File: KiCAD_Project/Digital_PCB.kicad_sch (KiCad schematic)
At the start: 40 parts, among them J1 NP_Conn_01x02_Relief, J10 1-0001156, J2 Board to Board, J3 1-0001156, J4 1-0001205, J5 NP_Conn_01x04, J6 NP_Conn_01x02_Relief, J7 NP_Conn_01x04, U1 1-0000207, Y1 1-0000721

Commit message: Schematic ERC Issue Cleanup
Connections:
- no-connect marks 12 -> 13
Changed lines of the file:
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@@
 	)
 	(no_connect
+		(at 119.38 91.44)
+	)
+	(no_connect
 		(at 152.4 119.38)
 	)
@@
 			"AAAAAAAAAAAAAAAAAAAAAAAAAAAAAAAAAAAAAAAAAAAAAAAAAAAAAAAAAAAAAAAAAAAAAAAAAAAA"
 			"AAAAAAAAAAAAAAAAAAAAAAAAAAAAAAAAAAAAAAAAAAAAAAAAAAAAAAAAAAAAAAAAAAAAAAAAAAAA"
+			"AAAAAAAAAAAAAAAAAAAAAAAAAAAAAAAAAAAAAAAAAAAAAAAAAAAAAAAAAAAAAAAAAAAAAAAAAAAA"
+			"AAAAAAAAAAAAAAAAAAAAAAAAAAAAAAAAAAAAAAAAAAAAAAAAAAAAAAAAAAAAAAAAAAAAAAAAAAAA"
+			"AAAAAAAAAAAAAAAAAAAAAAAAAAAAAAAAAAAAAAAAAAAAAAAAAAAAAAAAAAAAAAAAAAAAAAAAAAAA"
+			"AAAAAAAAAAAAAAAAAAAAAAAAAAAAAAAAAAAAAAAAAAAAAAAAAAAAAAAAAAAAAAAAAAAAAAAAAAAA"
+			"AAAAAAAAAAAAAAAAAAAAAAAAAAAAAAAAAAAAAAAAAAAAAAAAAAAAAAAAAAAAAAAAAAAAAAAAAAAA"
+			"AAAAAAAAAAAAAAAAAAAAAAAAAAAAAAAAAAAAAAAAAAAAAAAAAAAAAAAAAAAAAAAAAAAAAAAAAAAA"
+			"AAAAAAAAAAAAAAAAAAAAAAAAAAAAAAAAAAAAAAAAAAAAAAAAAAAAAAAAAAAAAAAAAAAAAAAAAAAA"
+			"AAAAAAAAAAAAAAAAAAAAAAAAAAAAAAAAAAAAAAAAAAAAAAAAAAAAAAAAAAAAAAAAAAAAAAAAAAAA"
+			"AAAAAAAAAAAAAAAAAAAAAAAAAAAAAAAAAAAAAAAAAAAAAAAAAAAAAAAAAAAAAAAAAAAAAAAAAAAA"
+			"AAAAAAAAAAAAAAAAAAAAAAAAAAAAAAAAAAAAAAAAAAAAAAAAAAAAAAAAAAAAAAAAAAAAAAAAAAAA"
+			"AAAAAAAAAAAAAAAAAAAAAAAAAAAAAAAAAAAAAAAAAAAAAAAAAAAAAAAAAAAAAAAAAAAAAAAAAAAA"
+			"AAAAAAAAAAAAAAAAAAAAAAAAAAAAAAAAAAAAAAAAAAAAAAAAAAAAAAAAAAAAAAAAAAAAAAAAAAAA"
+			"AAAAAAAAAAAAAAAAAAAAAAAAAAAAAAAAAAAAAAAAAAAAAAAAAAAAAAAAAAAAAAAAAAAAAAAAAAAA"
+			"AAAAAAAAAAAAAAAAAAAAAAAAAAAAAAAAAAAAAAAAAAAAAAAAAAAAAAAAAAAAAAAAAAAAAAAAAAAA"
+			"AAAAAAAAAAAAAAAAAAAAAAAAAAAAAAAAAAAAAAAAAAAAAAAAAAAAAAAAAAAAAAAAAAAAAAAAAAAA"
+			"AAAAAAAAAAAAAAAAAAAAAAAAAAAAAAAAAAAAAAAAAAAAAAAAAAAAAAAAAAAAAAAAAAAAAAAAAAAA"
+			"AAAAAAAAAAAAAAAAAAAAAAAAAAAAAAAAAAAAAAAAAAAAAAAAAAAAAAAAAAAAAAAAAAAAAAAAAAAA"
+			"AAAAAAAAAAAAAAAAAAAAAAAAAAAAAAAAAAAAAAAAAAAAAAAAAAAAAAAAAAAAAAAAAAAAAAAAAAAA"
 			"AAAAAAAAAA=="
 		)
@@
 	(symbol
 		(lib_id "power:PWR_FLAG")
-		(at -22.86 194.31 0)
+		(at 5.08 19.05 0)
 		(unit 1)
 		(exclude_from_sim no)
@@
 		(fields_autoplaced yes)
 		(property "Reference" "#FLG04"
-			(at -22.86 192.405 0)
+			(at 5.08 17.145 0)
 			(effects
 				(font
@@
 		)
 		(property "Value" "PWR_FLAG"
-			(at -22.86 189.23 0)
+			(at 5.08 13.97 0)
 			(effects
 				(font
@@
 		)
 		(property "Footprint" ""
-			(at -22.86 194.31 0)
+			(at 5.08 19.05 0)
 			(effects
 				(font
@@
 		)
 		(property "Datasheet" "~"
-			(at -22.86 194.31 0)
+			(at 5.08 19.05 0)
 			(effects
 				(font
@@
 		)
 		(property "Description" "Special symbol for telling ERC where power comes from"
-			(at -22.86 194.31 0)
+			(at 5.08 19.05 0)
 			(effects
 				(font
@@
 	(symbol
 		(lib_id "power:GND")
-		(at -22.86 194.31 0)
+		(at 5.08 19.05 0)
 		(unit 1)
 		(exclude_from_sim no)
@@
 		(dnp no)
 		(property "Reference" "#PWR052"
-			(at -22.86 200.66 0)
+			(at 5.08 25.4 0)
 			(effects
 				(font
@@
 		)
 		(property "Value" "GND"
-			(at -22.733 198.7042 0)
+			(at 5.207 23.4442 0)
 			(effects
 				(font
@@
 		)
 		(property "Footprint" ""
-			(at -22.86 194.31 0)
+			(at 5.08 19.05 0)
 			(effects
 				(font
@@
 		)
 		(property "Datasheet" ""
-			(at -22.86 194.31 0)
+			(at 5.08 19.05 0)
 			(effects
 				(font
@@
 		)
 		(property "Description" "Power symbol creates a global label with name \"GND\" , ground"
-			(at -22.86 194.31 0)
+			(at 5.08 19.05 0)
 			(effects
 				(font

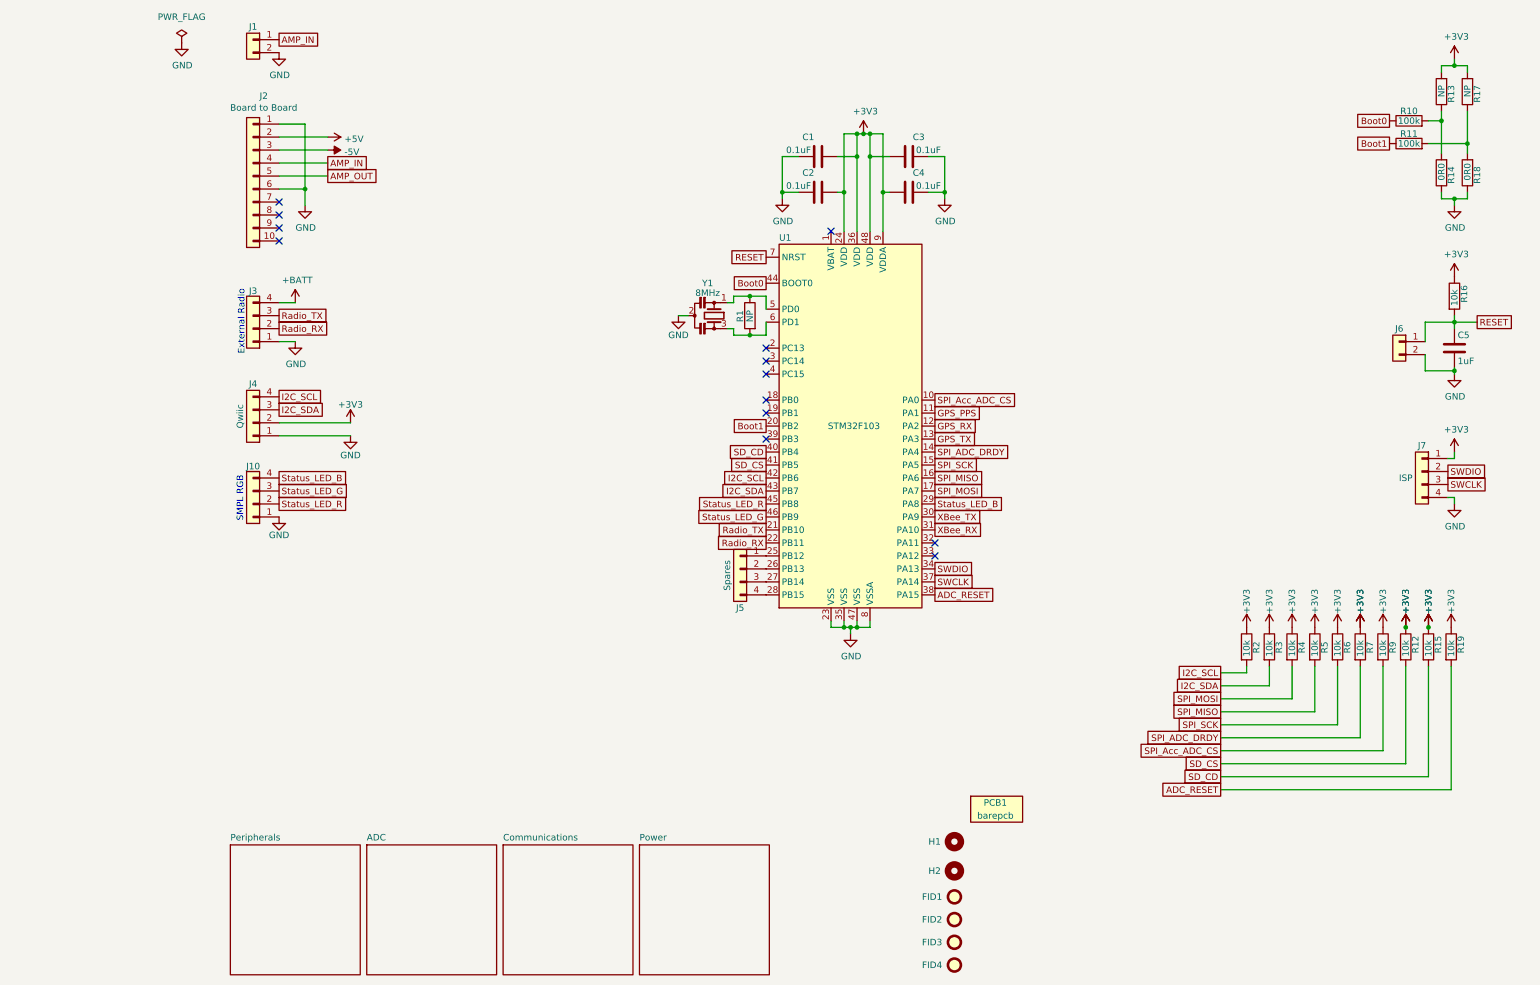
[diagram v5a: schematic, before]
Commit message: Revised Layout for Rev2.0 Changes
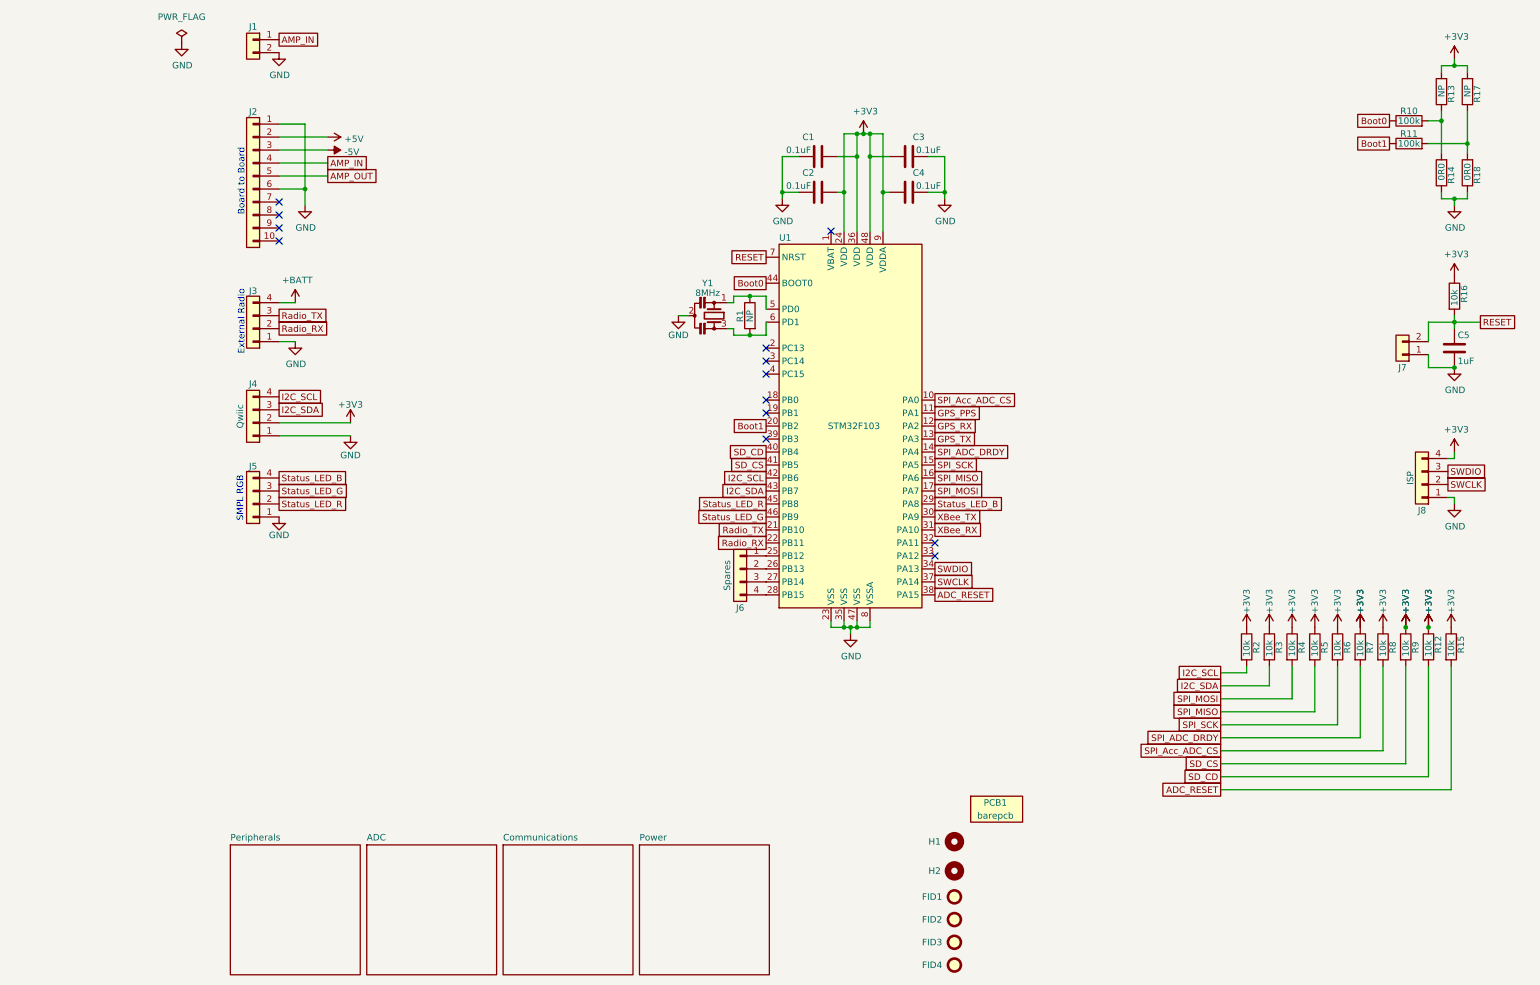
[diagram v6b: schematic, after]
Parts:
- PCB1: Internal Part Number 3-0000207 -> 3-0000270
- renumbered J10 to J5, J5 to J6, J6 to J7, J7 to J8, R15 to R12, R19 to R15, R9 to R8, R12 to R9
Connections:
- net +3V3: now also J8.4 (Pin_4); no longer J8.1 (Pin_1)
- net GND: now also J7.1 (Pin_1), J8.1 (Pin_1); no longer J7.2 (Pin_2), J8.4 (Pin_4)
- net RESET: now also J7.2 (Pin_2); no longer J7.1 (Pin_1)
- net SWCLK: now also J8.2 (Pin_2); no longer J8.3 (Pin_3)
- net SWDIO: now also J8.3 (Pin_3); no longer J8.2 (Pin_2)
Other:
- note added: "Board to Board"
- moved on the sheet: J7, J8

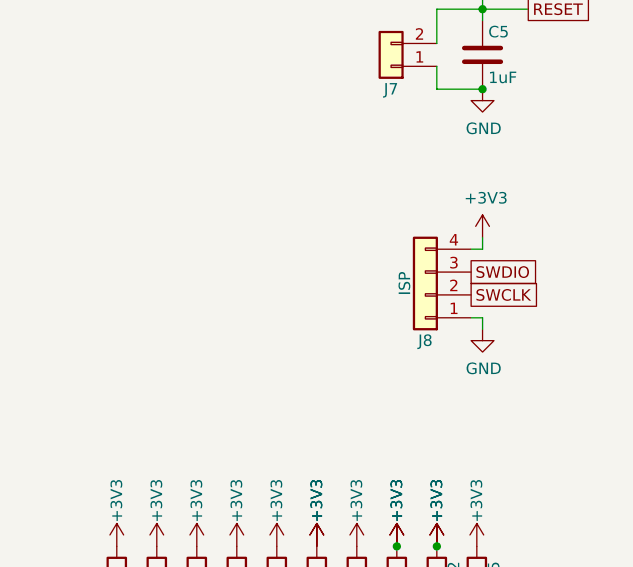
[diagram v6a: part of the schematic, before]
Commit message: Update ICSP label
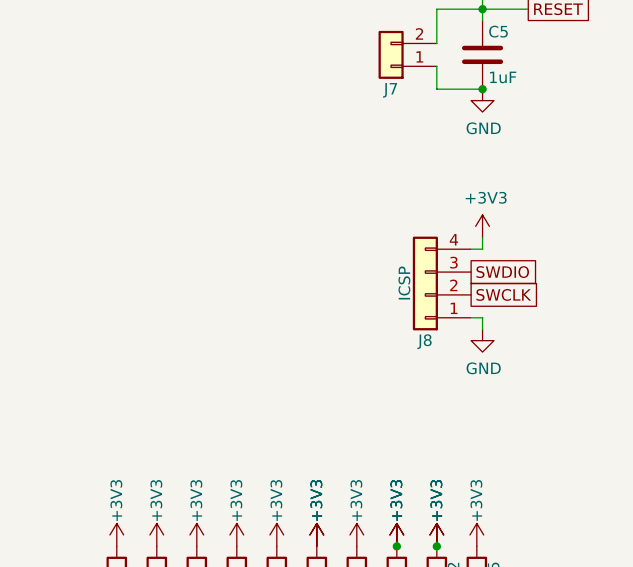
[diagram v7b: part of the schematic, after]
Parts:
- J8: PValue ISP -> ICSP
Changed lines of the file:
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@@
 			"802Z9gEAAG50Q2hhbmdlVHlwZUV4AFZhcmlhbnRDbGVhcgBWYXJpYW50Q29weQAGAAAG0V4sANDG"
 			"GA33AQAAAFFQmfYBAABpdABWYXJpYW50VGltZVRvRG9zRGF0ZVRpbWUAVmFyaWFudFRpbWVUb1N5"
-			"c3RlbVRpbQ=="
+			"c3RlbVRpbQAAAAAAAAAAAAAAAAAAAAAAAAAAAAAAAAAAAAAAAAAAAAAAAAAAAAAAAAAAAAAAAAAA"
+			"AAAAAAAAAAAAAAAAAAAAAAAAAAAAAAAAAAAAAAAAAAAAAAAAAAAAAAAAAAAAAAAAAAAAAAAAAAAA"
+			"AAAAAAAAAAAAAAAAAAAAAAAAAAAAAAAAAAAAAAAAAAAAAAAAAAAAAAAAAAAAAAAAAAAAAAAAAAAA"
+			"AAAAAAAAAAAAAAAAAAAAAAAAAAAAAAAAAAAAAAAAAAAAAAAAAAAAAAAAAAAAAAAAAAAAAAAAAAAA"
+			"AAAAAAAAAAAAAAAAAAAAAAAAAAAAAAAAAAAAAAAAAAAAAAAAAAAAAAAAAAAAAAAAAAAAAAAAAAAA"
+			"AAAAAAAAAAAAAAAAAAAAAAAAAAAAAAAAAAAAAAAAAAAAAAAAAAAAAAAAAAAAAAAAAAAAAAAAAAAA"
+			"AAAAAAAAAAAAAAAAAAAAAAAAAAAAAAAAAAAAAAAAAAAAAAAAAAAAAAAAAAAAAAAAAAAAAAAAAAAA"
+			"AAAAAAAAAAAAAAAAAAAAAAAAAAAAAAAAAAAAAAAAAAAAAAAAAAAAAAAAAAAAAAAAAAAAAAAAAAAA"
+			"AAAAAAAAAAAAAAAAAAAAAAAAAAAAAAAAAAAAAAAAAAAAAAAAAAAAAAAAAAAAAAAAAAAAAAAAAAAA"
+			"AAAAAAAAAAAAAAAAAAAAAAAAAAAAAAAAAAAAAAAAAAAAAAAAAAAAAAAAAAAAAAAAAAAAAAAAAAAA"
+			"AAAAAAAAAAAAAAAAAAAAAAAAAAAAAAAAAAAAAAAAAAAAAAAAAAAAAAAAAAAAAAAAAAAAAAAAAAAA"
+			"AAAAAAAAAAAAAAAAAAAAAAAAAAAAAAAAAAAAAAAAAAAAAAAAAAAAAAAAAAAAAAAAAAAAAAAAAAAA"
+			"AAAAAAAAAAAAAAAAAAAAAAAAAAAAAAAAAAAAAAAAAAAAAAAAAAAAAAAAAAAAAAAAAAAAAAAAAAAA"
+			"AAAAAAAAAAAAAAAAAAAAAAAAAAAAAAAAAAAAAAAAAAAAAAAAAAAAAAAAAAAAAAAAAAAAAAAAAAAA"
+			"AAAAAAAAAAAAAAAAAAAAAAAAAAAAAAAAAAAAAAAAAAAAAAAAAAAAAAAAAAAAAAAAAAAAAAAAAAAA"
+			"AAAAAAAAAAAAAAAAAAAAAAAAAAAAAAAAAAAAAAAAAAAAAAAAAAAAAAAAAAAAAAAAAAAAAAAAAAAA"
+			"AAAAAAAAAAAAAAAAAAAAAAAAAAAAAAAAAAAAAAAAAAAAAAAAAAAAAAAAAAAAAAAAAAAAAAAAAAAA"
+			"AAAAAAAAAAAAAAAAAAAAAAAAAAAAAAAAAAAAAAAAAAAAAAAAAAAAAAAAAAAAAAAAAAAAAAAAAAAA"
+			"AAAAAAAAAA=="
 		)
 	)
@@
 			)
 		)
-		(property "PValue" "ISP"
+		(property "PValue" "ICSP"
 			(at 245.364 104.14 90)
 			(effects
